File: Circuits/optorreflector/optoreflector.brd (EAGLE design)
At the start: 24 x 20 mm, 9 parts, among them IC1 LM358D

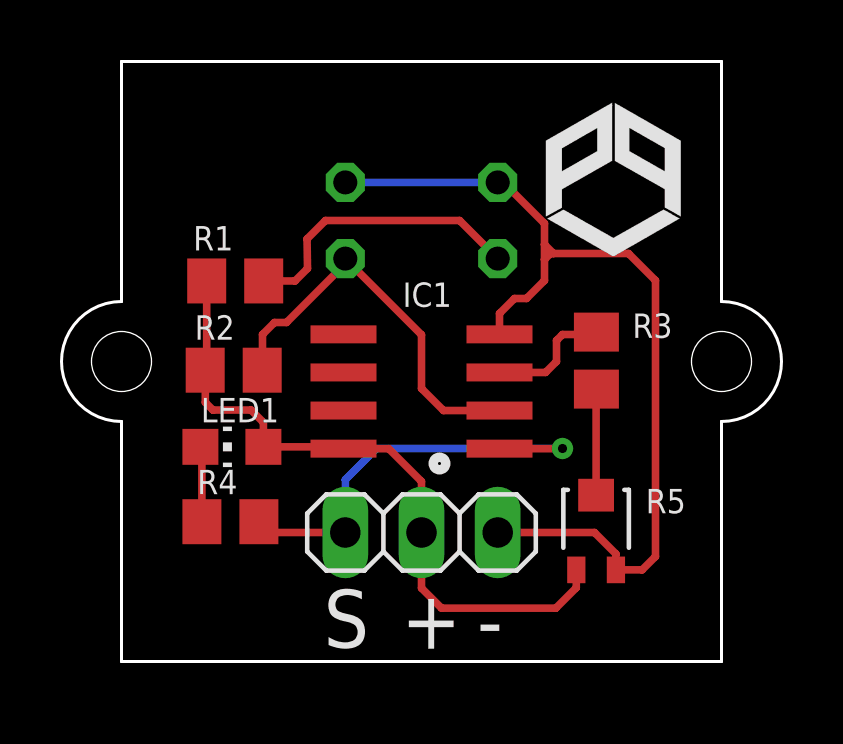
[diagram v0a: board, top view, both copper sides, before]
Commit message: ❌ Deleted unused files
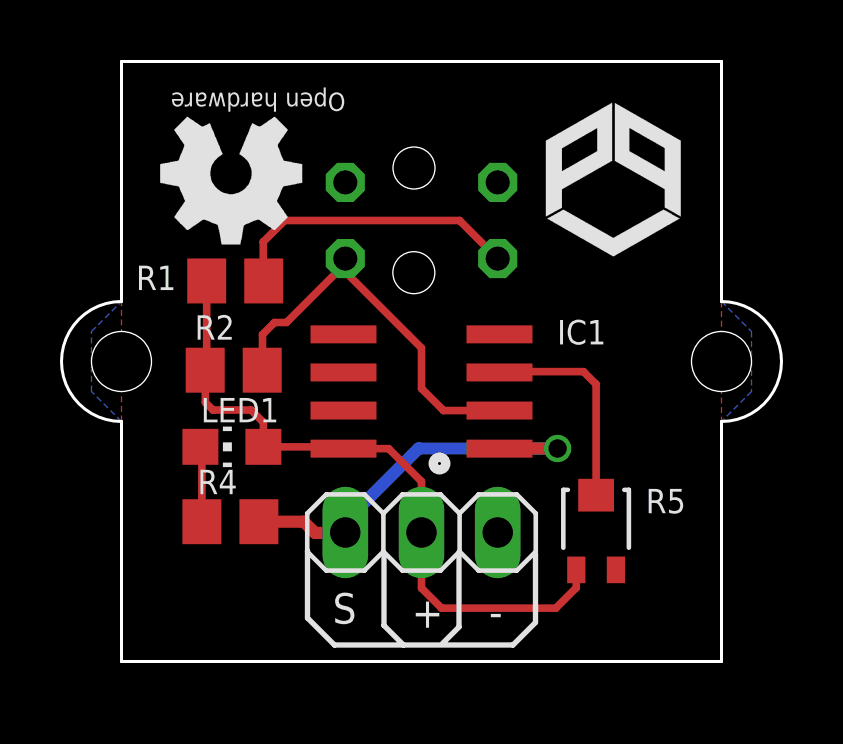
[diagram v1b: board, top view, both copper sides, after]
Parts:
- removed R3: 10k, rcl:R0805
- OS1: value (none) -> TCRT5000
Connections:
- net OUTPUT renamed N$5
- removed net N$5 (its old number): IC1.3, R3.1
- net N$4: now also IC1.3; no longer R3.2
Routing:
- net GND: track 31.8 -> 0.00 mm
- net N$5 (its old number): track 4.20 -> 0.00 mm
- net N$4: track 3.54 -> 7.10 mm
- net N$5: track 14.8 -> 13.4 mm
- added copper zone on layer 1, net GND
- added copper zone on layer 16, net GND
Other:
- board text added: "BD Team 2016 bilbaodynamics.com"
- board text added: "Open hardware"
